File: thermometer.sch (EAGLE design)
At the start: 36 parts, among them IC1 MAX232, Q2 54M10AUM1, T1 BC547, T2 BC547, T3 BC547, T6 BC547, T7 BC547, T8 BC547, T9 BC547, X2 MINI-USB_SHIELD4P-85-32004-10X

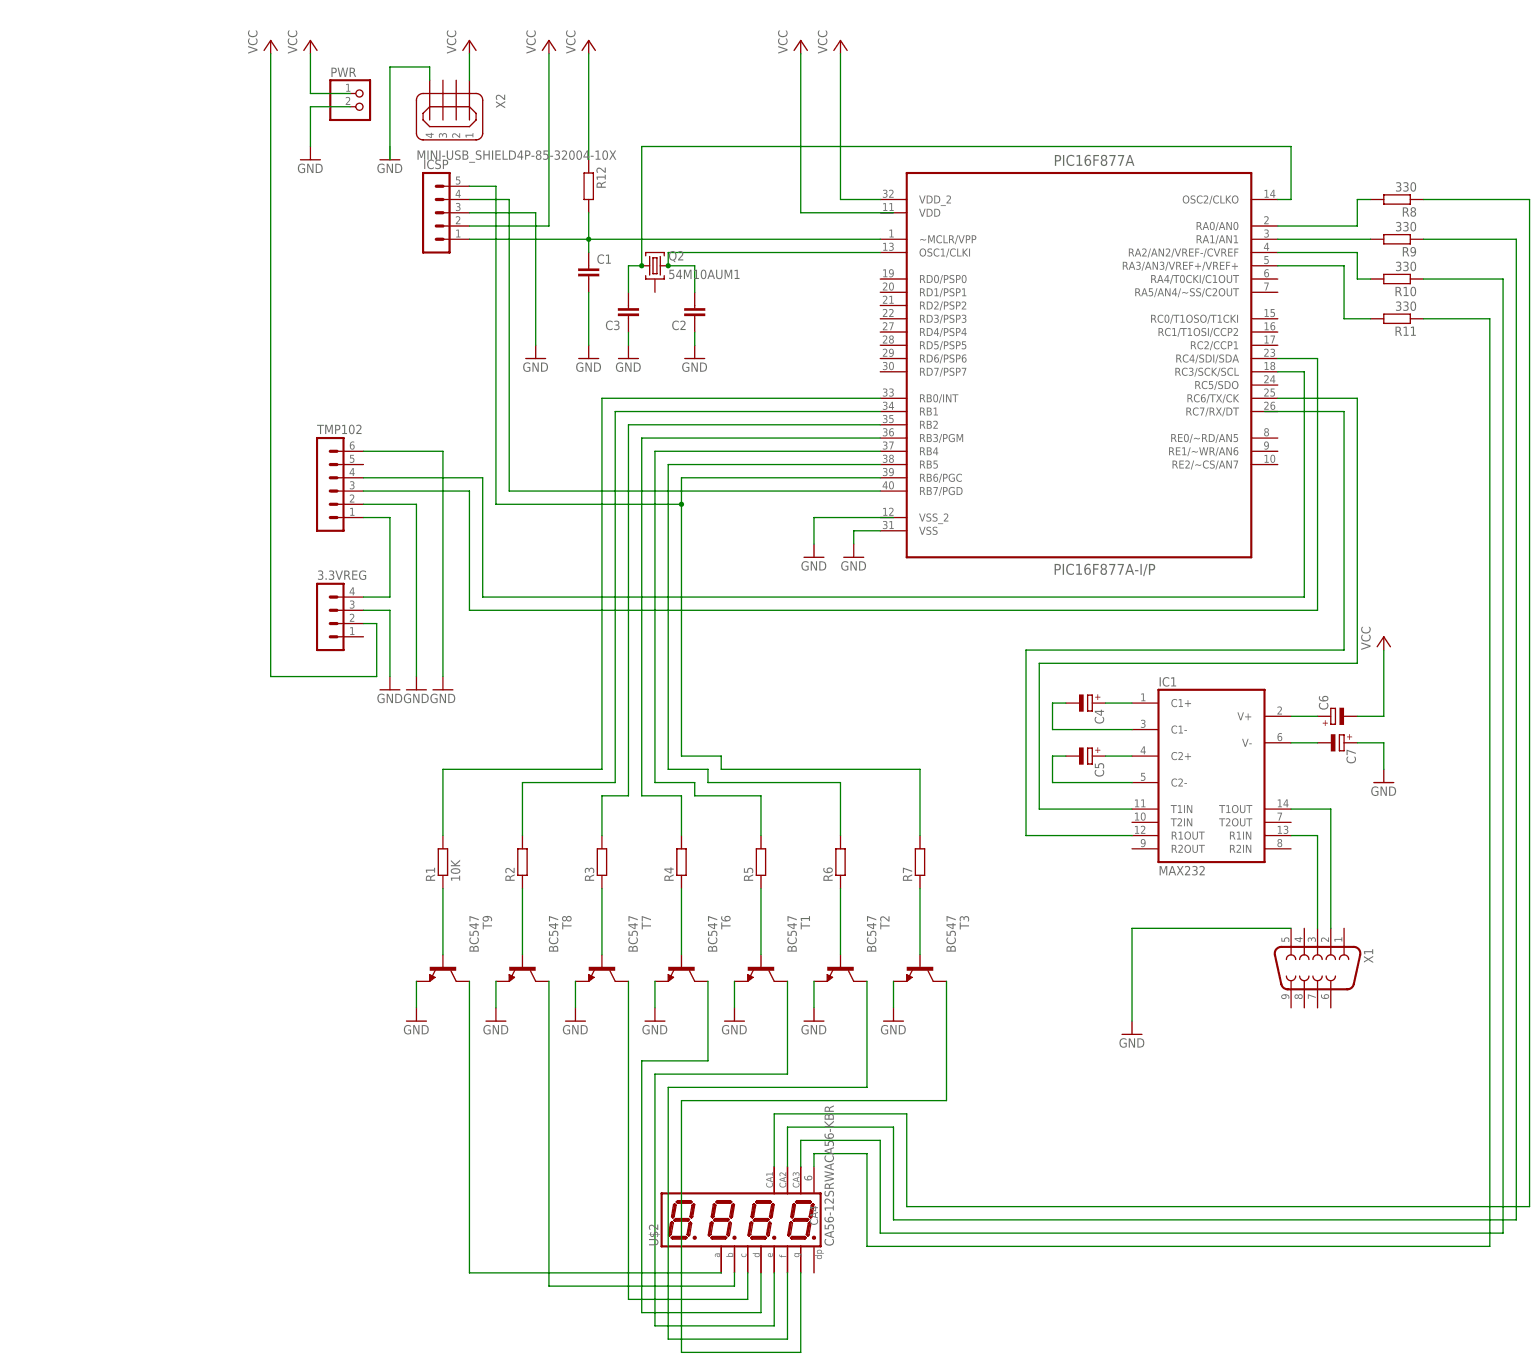
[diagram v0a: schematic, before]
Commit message: v 1.1 released. Several bug fixes
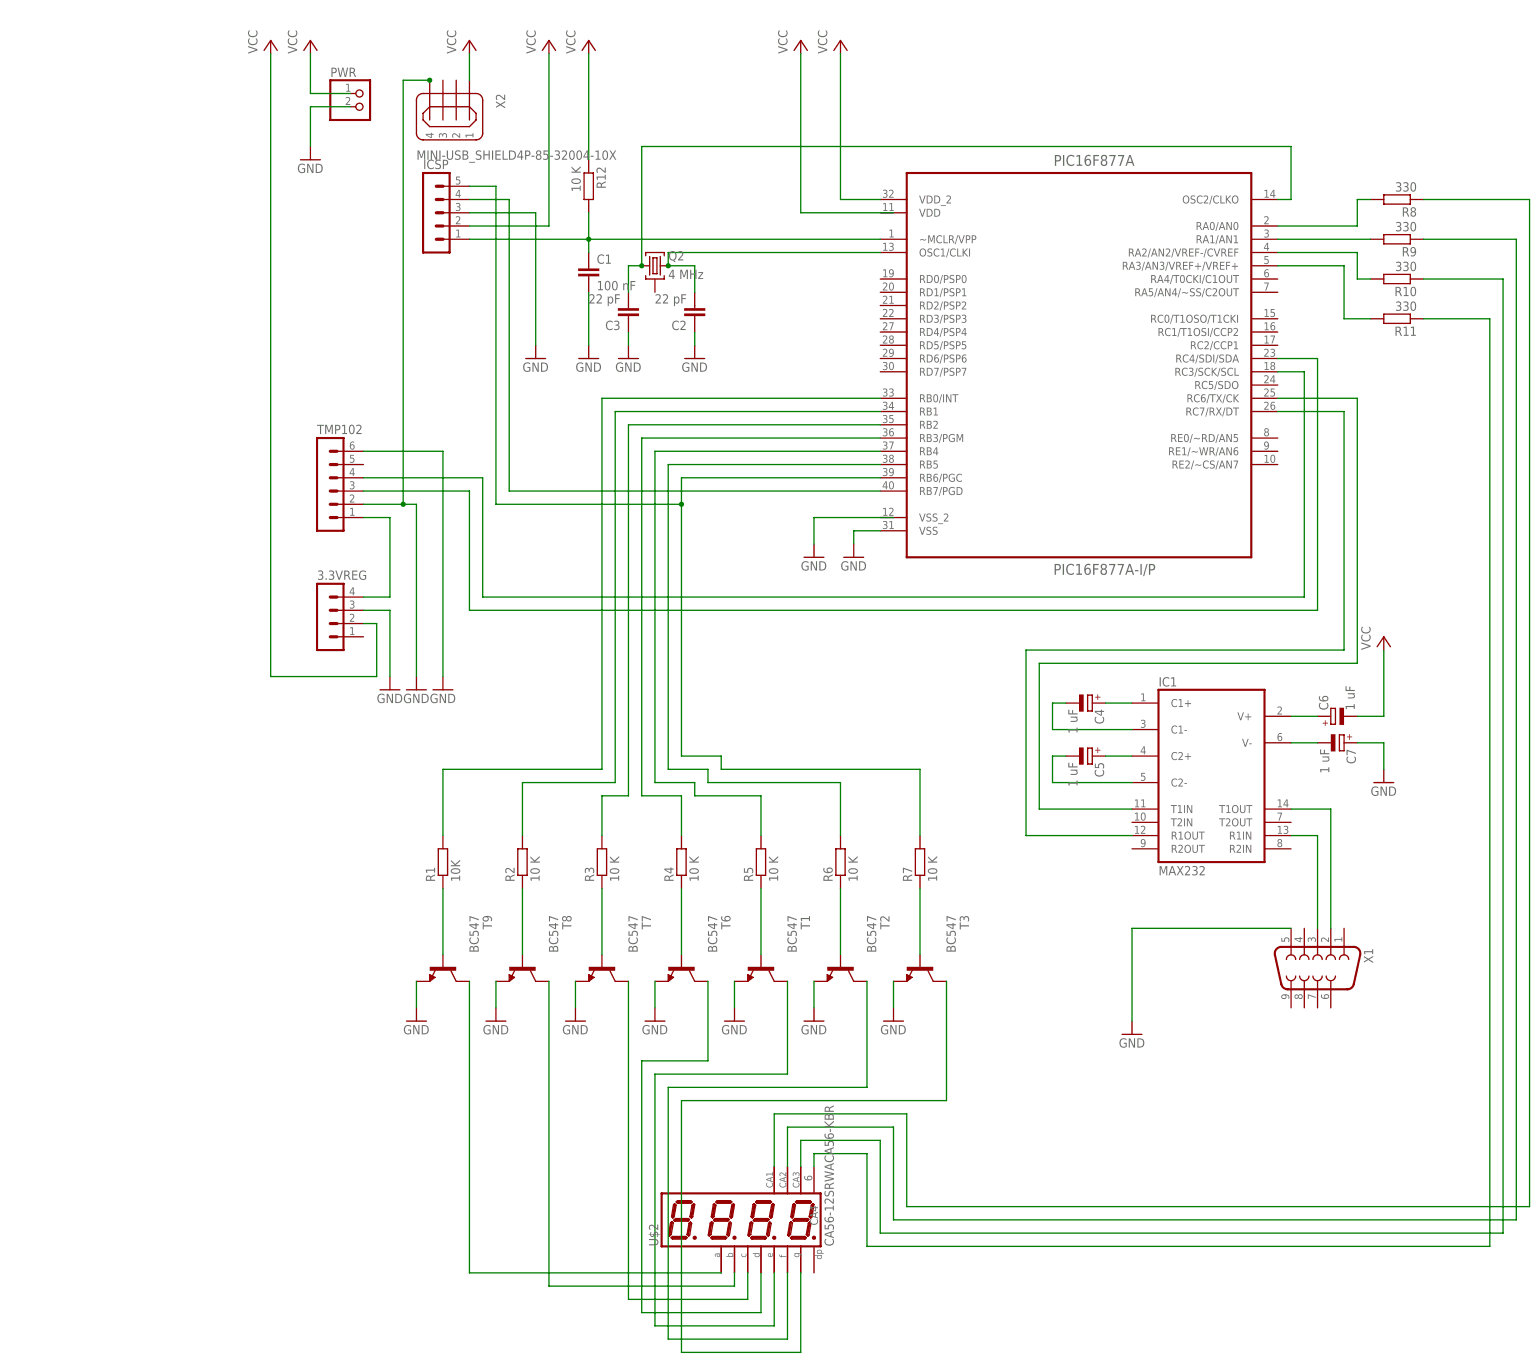
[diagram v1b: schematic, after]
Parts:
- C1: value (none) -> 100 nF; device rcl:C-EU025-025X050 -> rcl:C-EU050-025X075
- C2, C3: value (none) -> 22 pF; device rcl:C-EU025-025X050 -> rcl:C-EU050-025X075
- C4, C5, C6, C7: value (none) -> 1 uF; device rcl:CPOL-EUE5-8.5 -> rcl:CPOL-EUE1.8-4
- Q2: value 54M10AUM1 -> 4 MHz
- R12, R2, R3, R4, R5, R6, R7: value (none) -> 10 K
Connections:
- removed net N$46: X2G$1.4
- new net N$47: T8.C, U$2.B
- net GND: now also X2G$1.4
- net N$23: no longer T8.C, U$2.B
- net N$45: now also PIC16F877A.RC7/RX/DT
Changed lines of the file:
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@@
 <part name="T9" library="transistor" deviceset="BC547" device=""/>
 <part name="R1" library="eagle-ltspice" deviceset="R" device="0207/10" value="10K"/>
-<part name="R2" library="eagle-ltspice" deviceset="R" device="0207/10"/>
-<part name="R3" library="eagle-ltspice" deviceset="R" device="0207/10"/>
-<part name="R4" library="eagle-ltspice" deviceset="R" device="0207/10"/>
-<part name="R5" library="eagle-ltspice" deviceset="R" device="0207/10"/>
-<part name="R6" library="eagle-ltspice" deviceset="R" device="0207/10"/>
-<part name="R7" library="eagle-ltspice" deviceset="R" device="0207/10"/>
+<part name="R2" library="eagle-ltspice" deviceset="R" device="0207/10" value="10 K"/>
+<part name="R3" library="eagle-ltspice" deviceset="R" device="0207/10" value="10 K"/>
+<part name="R4" library="eagle-ltspice" deviceset="R" device="0207/10" value="10 K"/>
+<part name="R5" library="eagle-ltspice" deviceset="R" device="0207/10" value="10 K"/>
+<part name="R6" library="eagle-ltspice" deviceset="R" device="0207/10" value="10 K"/>
+<part name="R7" library="eagle-ltspice" deviceset="R" device="0207/10" value="10 K"/>
 <part name="GND1" library="supply1" deviceset="GND" device=""/>
 <part name="GND2" library="supply1" deviceset="GND" device=""/>
@@
 <part name="R10" library="resistor" deviceset="R-EU_" device="0204/7" value="330"/>
 <part name="R11" library="resistor" deviceset="R-EU_" device="0204/7" value="330"/>
-<part name="R12" library="rcl" deviceset="R-EU_" device="0204/7"/>
-<part name="C1" library="rcl" deviceset="C-EU" device="025-025X050"/>
-<part name="C2" library="rcl" deviceset="C-EU" device="025-025X050"/>
-<part name="C3" library="rcl" deviceset="C-EU" device="025-025X050"/>
+<part name="R12" library="rcl" deviceset="R-EU_" device="0204/7" value="10 K"/>
+<part name="C1" library="rcl" deviceset="C-EU" device="050-025X075" value="100 nF"/>
+<part name="C2" library="rcl" deviceset="C-EU" device="050-025X075" value="22 pF"/>
+<part name="C3" library="rcl" deviceset="C-EU" device="050-025X075" value="22 pF"/>
 <part name="GND8" library="supply1" deviceset="GND" device=""/>
 <part name="GND9" library="supply1" deviceset="GND" device=""/>
@@
 <part name="GND15" library="supply1" deviceset="GND" device=""/>
 <part name="GND16" library="supply1" deviceset="GND" device=""/>
-<part name="Q2" library="crystal" deviceset="54M10AUM1" device=""/>
+<part name="Q2" library="crystal" deviceset="54M10AUM1" device="" value="4 MHz"/>
 <part name="X1" library="con-subd" deviceset="F09" device="HP"/>
-<part name="C4" library="rcl" deviceset="CPOL-EU" device="E5-8.5"/>
-<part name="C5" library="rcl" deviceset="CPOL-EU" device="E5-8.5"/>
-<part name="C6" library="rcl" deviceset="CPOL-EU" device="E5-8.5"/>
-<part name="C7" library="rcl" deviceset="CPOL-EU" device="E5-8.5"/>
+<part name="C4" library="rcl" deviceset="CPOL-EU" device="E1.8-4" value="1 uF"/>
+<part name="C5" library="rcl" deviceset="CPOL-EU" device="E1.8-4" value="1 uF"/>
+<part name="C6" library="rcl" deviceset="CPOL-EU" device="E1.8-4" value="1 uF"/>
+<part name="C7" library="rcl" deviceset="CPOL-EU" device="E1.8-4" value="1 uF"/>
 <part name="IC1" library="maxim" deviceset="MAX232" device=""/>
 <part name="P+6" library="supply1" deviceset="VCC" device=""/>
@@
 <part name="X2" library="con-cypressindustries" deviceset="MINI-USB_SHIELD4P-" device="85-32004-10X"/>
 <part name="P+8" library="supply1" deviceset="VCC" device=""/>
-<part name="GND20" library="supply1" deviceset="GND" device=""/>
 </parts>
 <sheets>
@@
 <instance part="GND15" gate="1" x="-58.42" y="119.38"/>
 <instance part="GND16" gate="1" x="-53.34" y="119.38"/>
-<instance part="Q2" gate="G$1" x="-12.7" y="200.66"/>
+<instance part="Q2" gate="G$1" x="-12.7" y="200.66" smashed="yes">
+<attribute name="NAME" x="-10.16" y="201.676" size="1.778" layer="95"/>
+<attribute name="VALUE" x="-10.16" y="198.12" size="1.778" layer="96"/>
+</instance>
 <instance part="X1" gate="G$1" x="114.3" y="66.04" rot="R270"/>
 <instance part="C4" gate="G$1" x="71.12" y="116.84" rot="R270"/>
@@
 <instance part="X2" gate="G$1" x="-53.34" y="231.14" rot="R270"/>
 <instance part="P+8" gate="VCC" x="-48.26" y="243.84"/>
-<instance part="GND20" gate="1" x="-63.5" y="220.98"/>
 </instances>
 <busses>
@@
 <pinref part="TMP102" gate="1" pin="2"/>
 <pinref part="GND15" gate="1" pin="GND"/>
-<wire x1="-68.58" y1="154.94" x2="-58.42" y2="154.94" width="0.1524" layer="91"/>
+<wire x1="-68.58" y1="154.94" x2="-60.96" y2="154.94" width="0.1524" layer="91"/>
+<wire x1="-60.96" y1="154.94" x2="-58.42" y2="154.94" width="0.1524" layer="91"/>
 <wire x1="-58.42" y1="154.94" x2="-58.42" y2="121.92" width="0.1524" layer="91"/>
+<pinref part="X2" gate="G$1" pin="4"/>
+<wire x1="-55.88" y1="236.22" x2="-60.96" y2="236.22" width="0.1524" layer="91"/>
+<wire x1="-60.96" y1="236.22" x2="-60.96" y2="154.94" width="0.1524" layer="91"/>
+<junction x="-60.96" y="154.94"/>
+<junction x="-55.88" y="236.22"/>
 </segment>
 <segment>
@@
 </segment>
 </net>
-<net name="N$23" class="0">
-<segment>
-<wire x1="0" y1="7.62" x2="-33.02" y2="7.62" width="0.1524" layer="91"/>
-<pinref part="T9" gate="G$1" pin="C"/>
-<wire x1="-33.02" y1="7.62" x2="-48.26" y2="7.62" width="0.1524" layer="91"/>
-<wire x1="-48.26" y1="7.62" x2="-48.26" y2="63.5" width="0.1524" layer="91"/>
-<wire x1="2.54" y1="7.62" x2="2.54" y2="5.08" width="0.1524" layer="91"/>
-<wire x1="2.54" y1="5.08" x2="-33.02" y2="5.08" width="0.1524" layer="91"/>
-<wire x1="-33.02" y1="5.08" x2="-33.02" y2="7.62" width="0.1524" layer="91"/>
-<pinref part="T8" gate="G$1" pin="C"/>
-<wire x1="-33.02" y1="7.62" x2="-33.02" y2="63.5" width="0.1524" layer="91"/>
-<pinref part="U$2" gate="G$1" pin="B"/>
-<pinref part="U$2" gate="G$1" pin="A"/>
-</segment>
-</net>
 <net name="N$25" class="0">
 <segment>
@@
 </segment>
 </net>
+<net name="N$44" class="0">
+<segment>
+<pinref part="IC1" gate="G$1" pin="R1IN"/>
+<pinref part="X1" gate="G$1" pin="3"/>
+<wire x1="109.22" y1="91.44" x2="114.3" y2="91.44" width="0.1524" layer="91"/>
+<wire x1="114.3" y1="91.44" x2="114.3" y2="73.66" width="0.1524" layer="91"/>
+</segment>
+</net>
+<net name="N$43" class="0">
+<segment>
+<pinref part="IC1" gate="G$1" pin="T1OUT"/>
+<pinref part="X1" gate="G$1" pin="2"/>
+<wire x1="109.22" y1="96.52" x2="116.84" y2="96.52" width="0.1524" layer="91"/>
+<wire x1="116.84" y1="96.52" x2="116.84" y2="73.66" width="0.1524" layer="91"/>
+</segment>
+</net>
+<net name="N$47" class="0">
+<segment>
+<pinref part="U$2" gate="G$1" pin="B"/>
+<wire x1="2.54" y1="7.62" x2="2.54" y2="5.08" width="0.1524" layer="91"/>
+<pinref part="T8" gate="G$1" pin="C"/>
+<wire x1="2.54" y1="5.08" x2="-33.02" y2="5.08" width="0.1524" layer="91"/>
+<wire x1="-33.02" y1="5.08" x2="-33.02" y2="63.5" width="0.1524" layer="91"/>
+</segment>
+</net>
+<net name="N$23" class="0">
+<segment>
+<pinref part="U$2" gate="G$1" pin="A"/>
+<pinref part="T9" gate="G$1" pin="C"/>
+<wire x1="0" y1="7.62" x2="-48.26" y2="7.62" width="0.1524" layer="91"/>
+<wire x1="-48.26" y1="7.62" x2="-48.26" y2="63.5" width="0.1524" layer="91"/>
+</segment>
+</net>
 <net name="N$45" class="0">
 <segment>
-<wire x1="104.14" y1="172.72" x2="119.38" y2="172.72" width="0.1524" layer="91"/>
+<pinref part="PIC16F877A" gate="A" pin="RC7/RX/DT"/>
+<wire x1="106.68" y1="172.72" x2="119.38" y2="172.72" width="0.1524" layer="91"/>
 <wire x1="119.38" y1="172.72" x2="119.38" y2="127" width="0.1524" layer="91"/>
 <wire x1="119.38" y1="127" x2="58.42" y2="127" width="0.1524" layer="91"/>
@@
 </segment>
 </net>
-<net name="N$44" class="0">
-<segment>
-<pinref part="IC1" gate="G$1" pin="R1IN"/>
-<pinref part="X1" gate="G$1" pin="3"/>
-<wire x1="109.22" y1="91.44" x2="114.3" y2="91.44" width="0.1524" layer="91"/>
-<wire x1="114.3" y1="91.44" x2="114.3" y2="73.66" width="0.1524" layer="91"/>
-</segment>
-</net>
-<net name="N$43" class="0">
-<segment>
-<pinref part="IC1" gate="G$1" pin="T1OUT"/>
-<pinref part="X1" gate="G$1" pin="2"/>
-<wire x1="109.22" y1="96.52" x2="116.84" y2="96.52" width="0.1524" layer="91"/>
-<wire x1="116.84" y1="96.52" x2="116.84" y2="73.66" width="0.1524" layer="91"/>
-</segment>
-</net>
-<net name="N$46" class="0">
-<segment>
-<wire x1="-63.5" y1="220.98" x2="-63.5" y2="238.76" width="0.1524" layer="91"/>
-<pinref part="X2" gate="G$1" pin="4"/>
-<wire x1="-63.5" y1="238.76" x2="-55.88" y2="238.76" width="0.1524" layer="91"/>
-<wire x1="-55.88" y1="238.76" x2="-55.88" y2="236.22" width="0.1524" layer="91"/>
-</segment>
-</net>
